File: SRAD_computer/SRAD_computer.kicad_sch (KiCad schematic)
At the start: 34 parts, among them J1 USB_B_Micro, J2 Conn_01x02, J3 Conn_02x18_Odd_Even, J4 Conn_02x18_Odd_Even, U1 NCP1117-3.3_SOT223, U2 W25Q128JVS, U3 RP2040, Y1 ABM8-272-T3

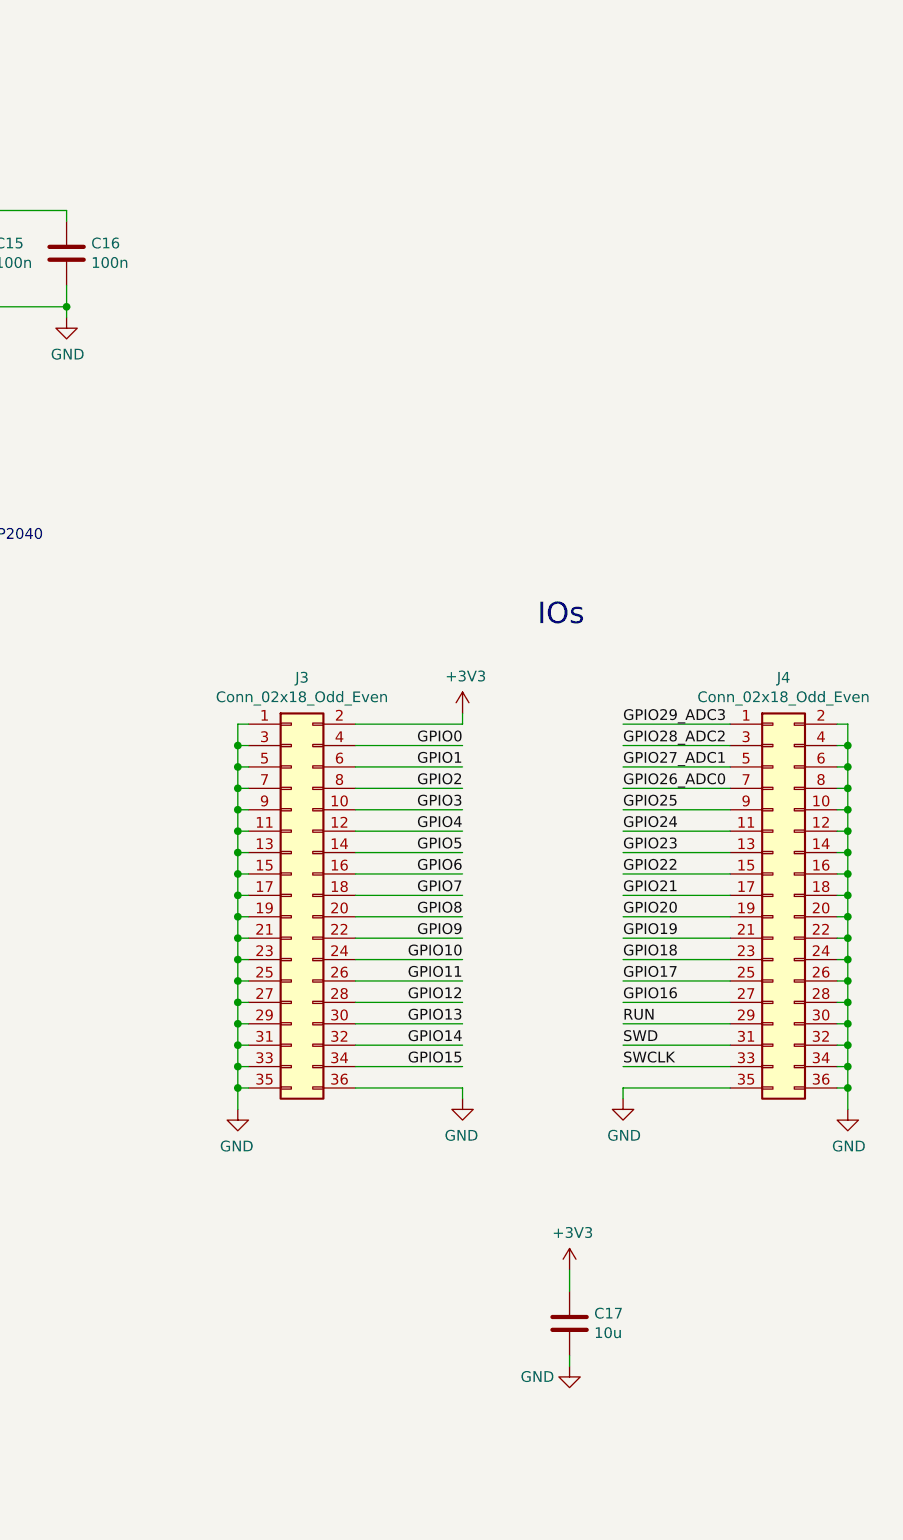
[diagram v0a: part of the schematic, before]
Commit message: RP2040 minimal components placed
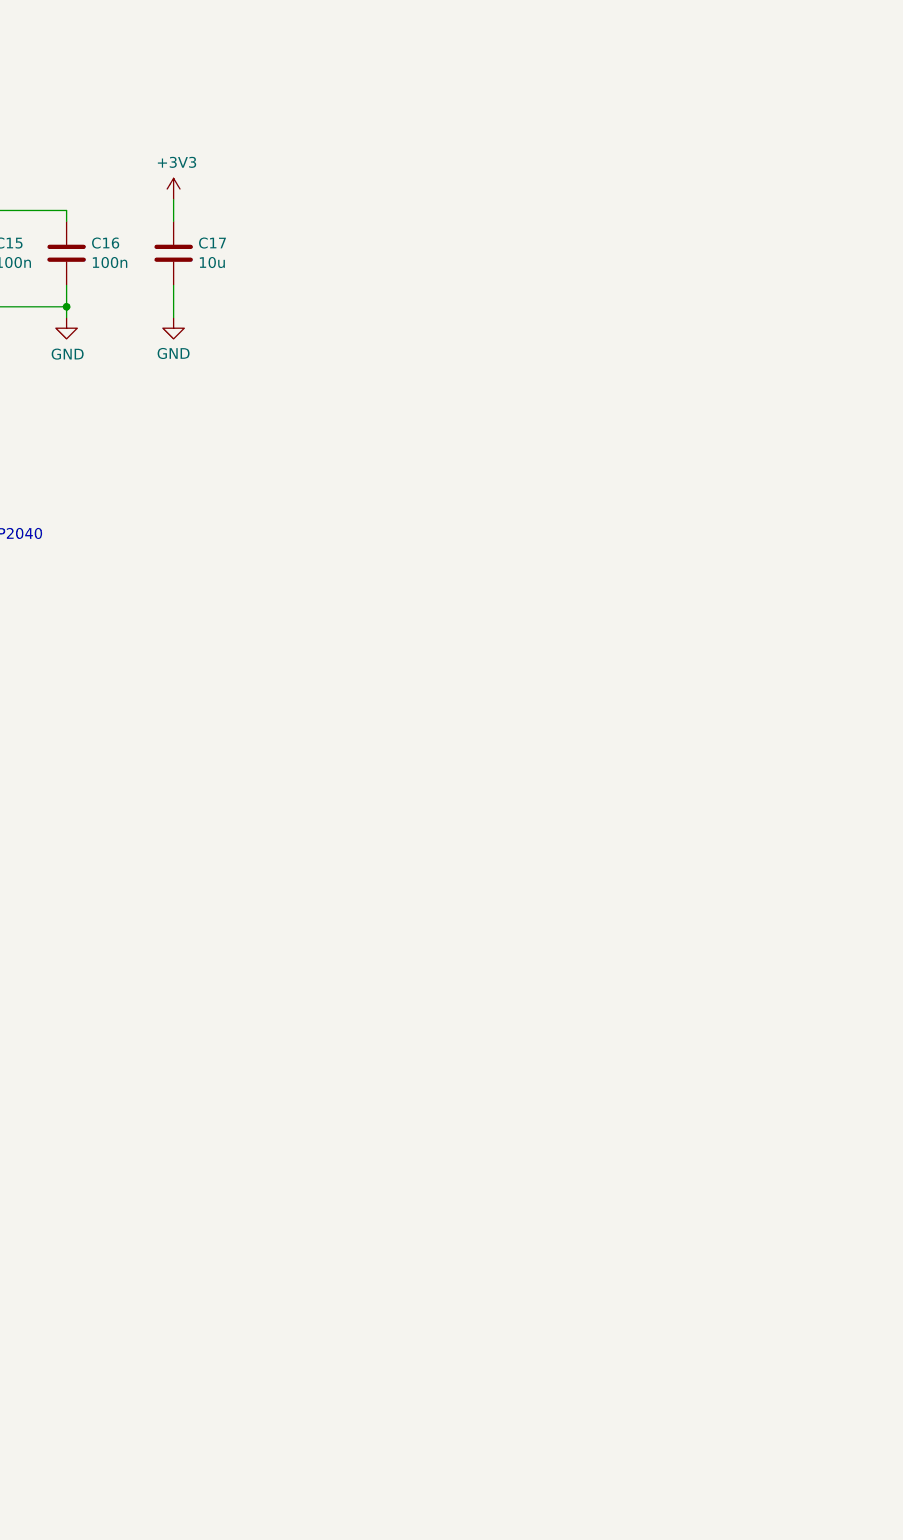
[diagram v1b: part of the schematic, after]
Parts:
- removed J3, J4: Conn_02x18_Odd_Even, Connector_PinHeader_2.54mm:PinHeader_2x18_P2.54mm_Vertical, symbol Connector_Generic:Conn_02x18_Odd_Even
- J1: footprint RP2040_minimal:USB_Micro-B_Amphenol_10103594-0001LF_Horizontal_modified -> RP2040_minimal_r2:USB_Micro-B_Amphenol_10103594-0001LF_Horizontal_modified
- R1, R2: footprint Resistor_SMD:R_0402_1005Metric -> Resistor_SMD:R_0805_2012Metric
- U2: footprint Package_SO:SOIC-8_5.23x5.23mm_P1.27mm -> Package_SO:SOIC-8_5.3x5.3mm_P1.27mm
- U3: footprint RP2040_minimal:RP2040-QFN-56 -> RP2040_minimal_r2:RP2040-QFN-56
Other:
- note removed: "IOs"
- moved on the sheet: C17

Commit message: schematic update: MPU, BME & SAM m8q
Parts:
- added C18, C_VDD_MPU: 100n, TCLib:C_5mm, symbol TCLib:C
- added C_BME_VDD: C, TCLib:C_0805, symbol TCLib:C
- added C_BME_VDDIO: C, TCLib:C_5mm, symbol TCLib:C
- added C_VDDIO_MPU: 10n, TCLib:C_5mm, symbol TCLib:C
- added R6, R_BME_SDA: R, TCLib:R_0805, symbol Device:R
- added R7, R_BME_SCL: R, symbol Device:R
- added U4: BME280, symbol Rocketry_FC:BME280
- added U5: MPU-9250, MPU-9250:QFN40P300X300X105-25N, symbol Rocketry_FC:MPU-9250
- added U6: SAM-M8Q-0-10, SAM-M8Q-0-10:MODULE_SAM-M8Q-0-10, symbol Rocketry_FC:SAM-M8Q-0-10
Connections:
- net GND: now also C18.2, C_BME_VDD.2, C_BME_VDDIO.2, C_VDDIO_MPU.2, C_VDD_MPU.2, U4.1 (GND), U4.7 (GND), U5.18 (GND), U5.20 (RESV_20)
- new net: C18.1, U5.10 (REGOUT)
- new net: U6.1 (GND), U6.10 (GND), U6.11 (GND), U6.15 (GND), U6.16 (GND), U6.20 (GND), U6.4 (GND), U6.5 (GND), U6.6 (GND)
- new net: U5.14 (NC), U5.15 (NC), U5.16 (NC), U5.17 (NC), U5.2 (NC), U5.3 (NC), U5.4 (NC), U5.5 (NC), U5.6 (NC)
- new net: R6.2, U5.23 (SCL/SCLK)
- new net: R7.2, U5.24 (SDA/SDI)
- new net +3.3V: C_BME_VDD.1, C_BME_VDDIO.1, C_VDDIO_MPU.1, C_VDD_MPU.1, R6.1, R7.1, R_BME_SCL.1, R_BME_SDA.1, U4.2 (CSB), U4.6 (VDDIO), U4.8 (VDD), U5.1 (RESV_1), U5.13 (VDD), U5.22 (~{CS}), U5.8 (VDDIO)
- new net BME_SCL: R_BME_SCL.2, U4.4 (SCK)
- new net BME_SDA: R_BME_SDA.2, U4.3 (SDI)
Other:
- note added: "BME280 Humidity and pressure sensor"
- note added: "MPU9250 Gyroscope & accelerometer"
- moved on the sheet: C10, C11, C12, C13, C14, C15, C16, C17, C6, C7, C8, C9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
